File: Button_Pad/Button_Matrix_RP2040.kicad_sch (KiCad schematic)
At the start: 38 parts, among them J1 Conn_01x03, J2 TYPE-C-31-M-12, J3 Conn_01x05, J4 Conn_01x09, U1 RP2040, U2 NCP1117-3.3_SOT223, U3 W25Q128JVS, U7 NCP1117-5.0_SOT223, Y1 X322512MSB4SI

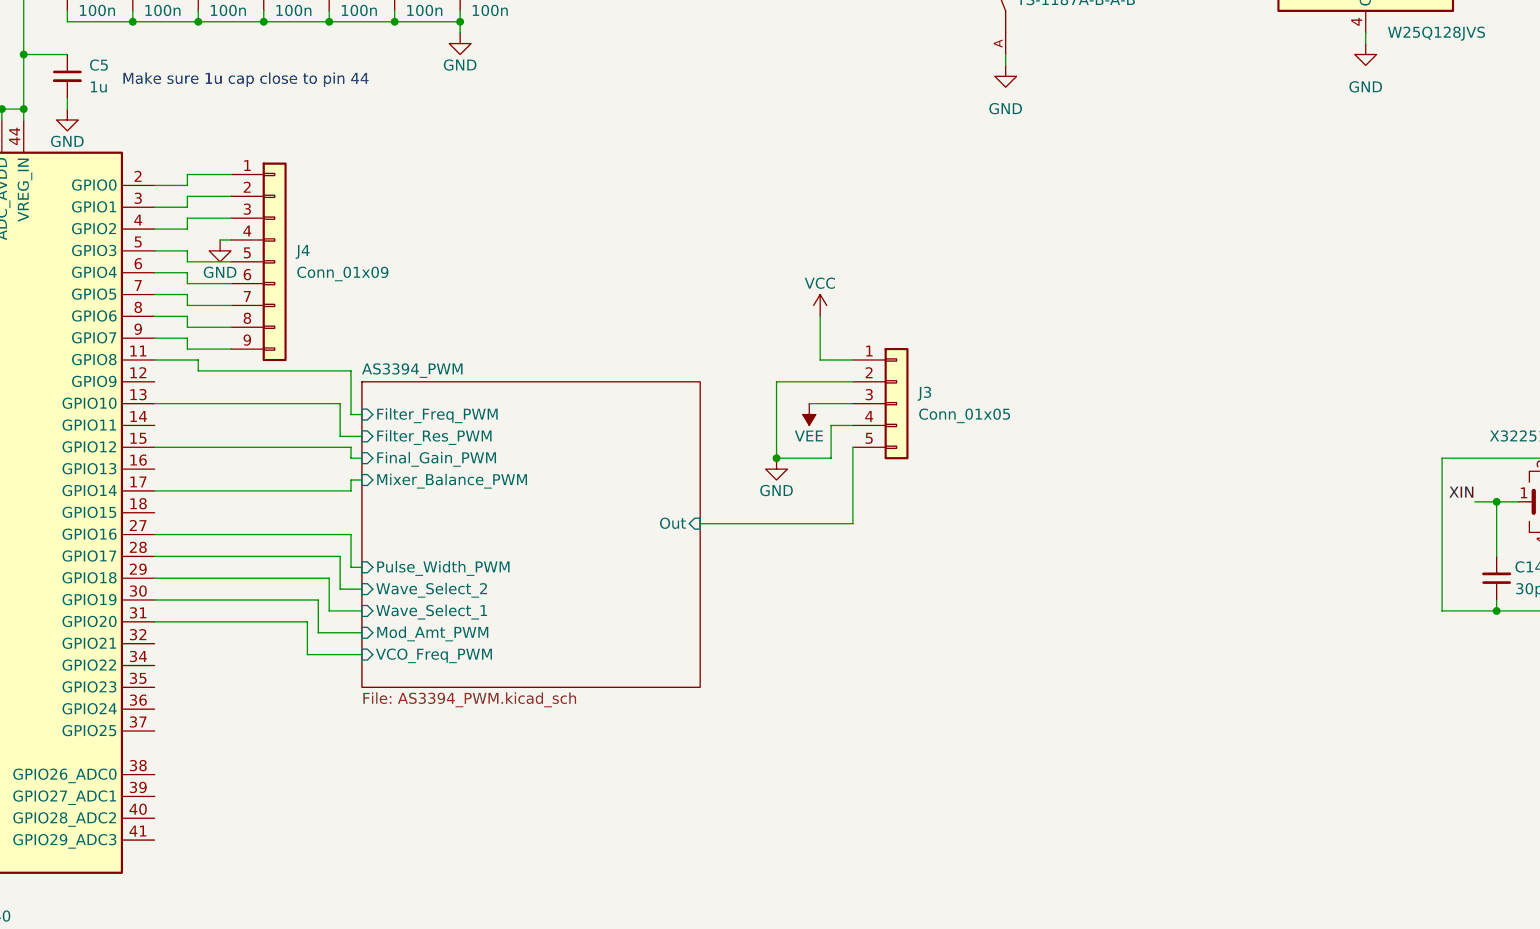
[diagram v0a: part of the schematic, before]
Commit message: added separate LDO for 3394, removed amp, designed psu board and made project for carrier board
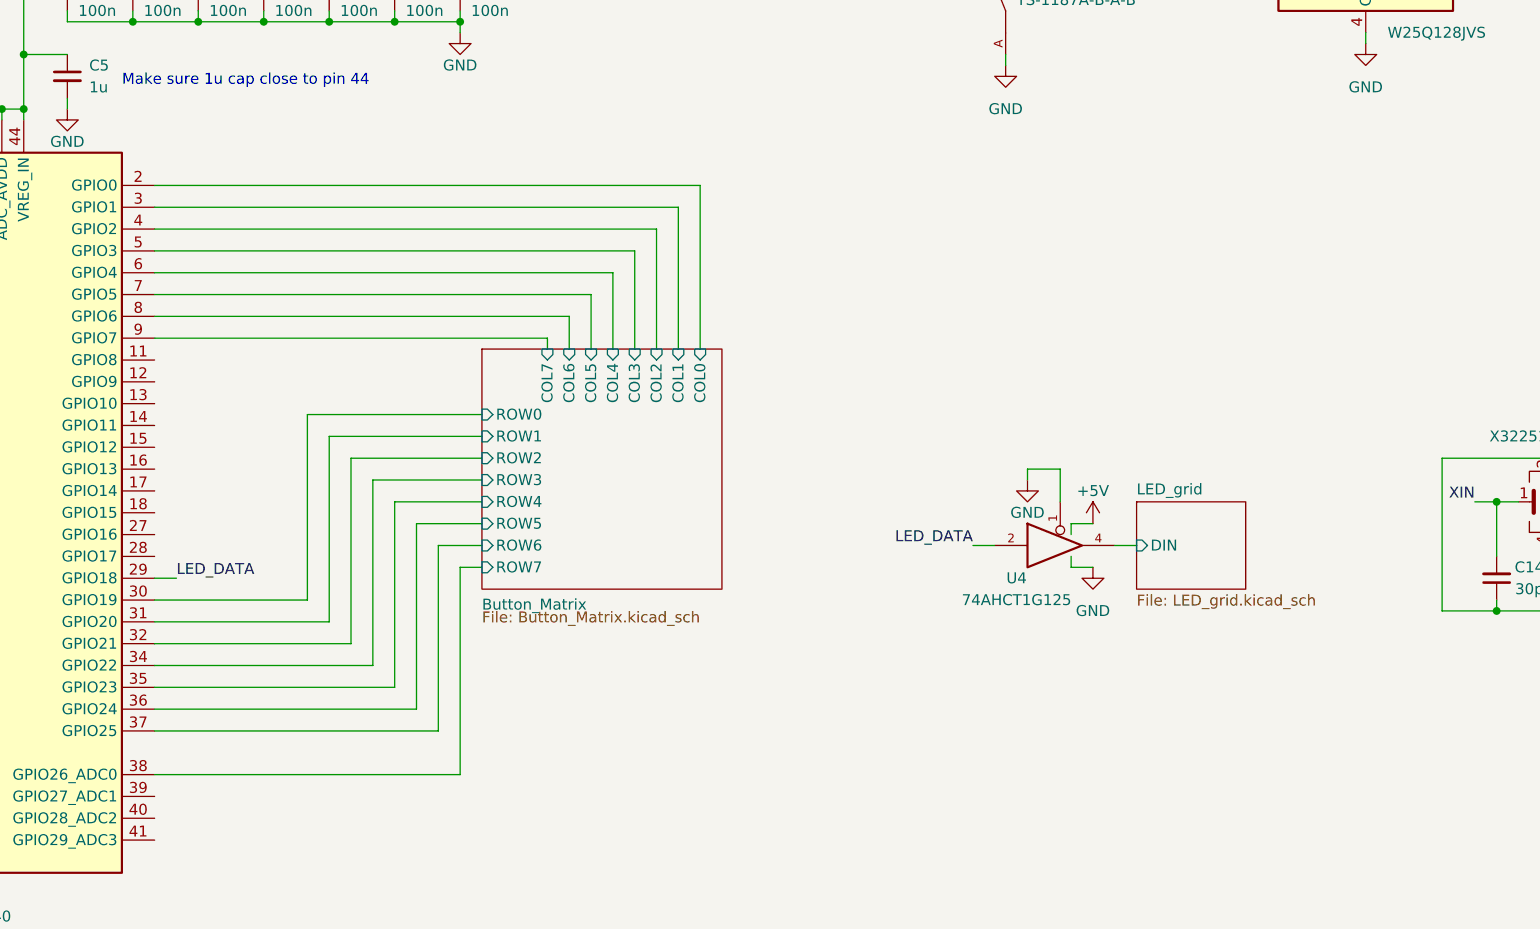
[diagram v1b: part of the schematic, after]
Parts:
- removed J3: Conn_01x05, Connector_PinHeader_2.54mm:PinHeader_1x05_P2.54mm_Vertical, symbol Connector_Generic:Conn_01x05
- removed J4: Conn_01x09, Connector_PinHeader_2.54mm:PinHeader_1x09_P2.54mm_Vertical, symbol Connector_Generic:Conn_01x09
- added U4: 74AHCT1G125, Package_TO_SOT_SMD:SOT-23-5, symbol 74xGxx:74AHCT1G125
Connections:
- net VCC is gone; now on net +5V: C50.1, D2.2 (A), U7.3 (VI)
- net +5V: now also U4.5 (VCC)
- net GND: now also U4.1, U4.3 (GND)
- net Button_Matrix/COL0: now reaches U1.2 (GPIO0)
- net Button_Matrix/COL1: now reaches U1.3 (GPIO1)
- net Button_Matrix/COL2: now reaches U1.4 (GPIO2)
- net Button_Matrix/COL3: now reaches U1.5 (GPIO3)
- net Button_Matrix/COL4: now reaches U1.6 (GPIO4)
- net Button_Matrix/COL5: now reaches U1.7 (GPIO5)
- net Button_Matrix/COL6: now reaches U1.8 (GPIO6)
- net Button_Matrix/COL7: now reaches U1.9 (GPIO7)
- net Button_Matrix/ROW2: now reaches U1.32 (GPIO21)
- net Button_Matrix/ROW3: now reaches U1.34 (GPIO22)
- net Button_Matrix/ROW4: now reaches U1.35 (GPIO23)
- net Button_Matrix/ROW5: now reaches U1.36 (GPIO24)
- net Button_Matrix/ROW6: now reaches U1.37 (GPIO25)
- net Button_Matrix/ROW7: now reaches U1.38 (GPIO26_ADC0)
- net AS3394_PWM/Filter_Freq_PWM: no longer names the net of U1.11 (GPIO8)
- net AS3394_PWM/Filter_Res_PWM: no longer names the net of U1.13 (GPIO10)
- net AS3394_PWM/Final_Gain_PWM: no longer names the net of U1.15 (GPIO12)
- net AS3394_PWM/Mixer_Balance_PWM: no longer names the net of U1.17 (GPIO14)
- net AS3394_PWM/Mod_Amt_PWM renamed Button_Matrix/ROW0
- net AS3394_PWM/Pulse_Width_PWM: no longer names the net of U1.27 (GPIO16)
- net AS3394_PWM/VCO_Freq_PWM renamed Button_Matrix/ROW1
- net AS3394_PWM/Wave_Select_1 renamed LED_DATA
- net LED_DATA: now also U4.2
- net AS3394_PWM/Wave_Select_2: no longer names the net of U1.28 (GPIO17)
- new net LED_grid/DIN: U4.4
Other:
- removed sheet AS3394_PWM
- added sheet Button_Matrix (Button_Matrix.kicad_sch)
- added sheet LED_grid (LED_grid.kicad_sch)
